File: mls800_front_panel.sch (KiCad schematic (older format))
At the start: 21 parts, among them SW10 SW_TACT_LED, SW11 SW_TACT_LED, SW2 SW_TACT_LED, SW3 SW_TACT_LED, SW4 SW_TACT_LED, SW5 SW_TACT_LED, SW6 SW_TACT_LED, SW7 SW_TACT_LED, SW8 SW_TACT_LED, SW9 SW_TACT_LED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

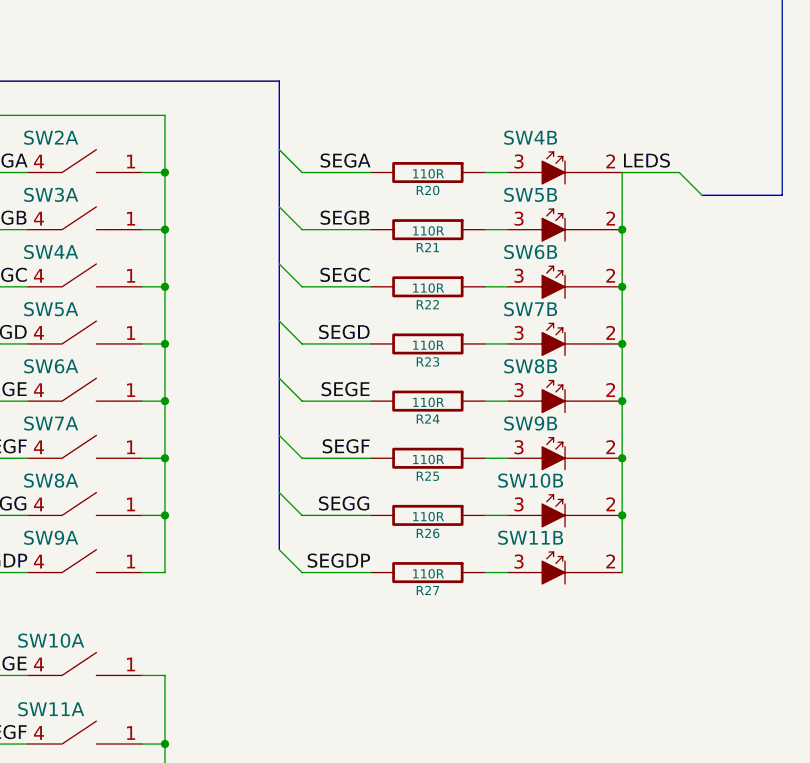
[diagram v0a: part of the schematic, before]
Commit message: MLS800
* removed front panel leds resistances
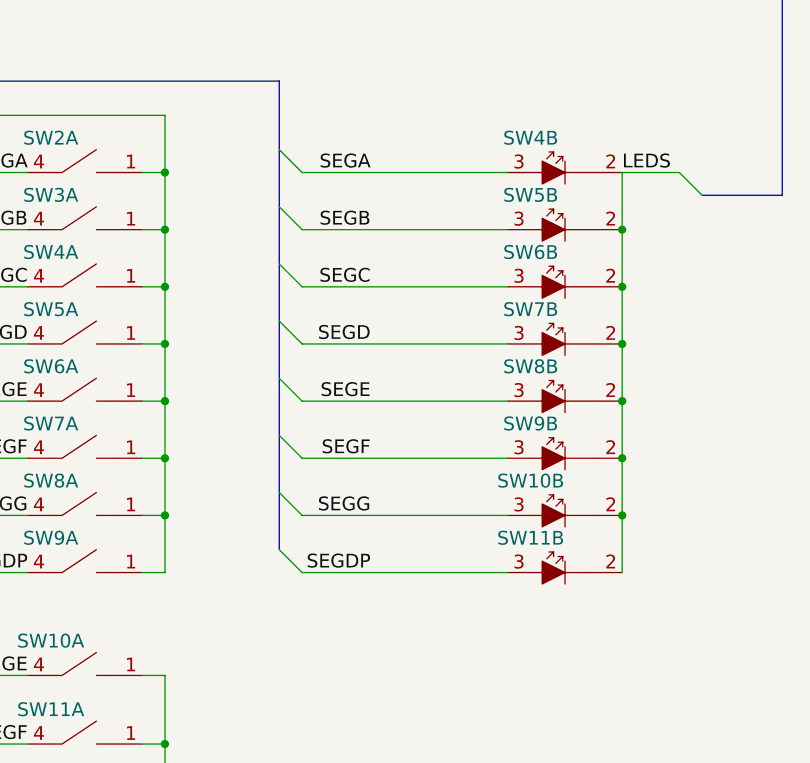
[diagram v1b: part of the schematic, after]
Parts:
- removed R20, R21, R22, R23, R24, R25, R26, R27: 110R, symbol R
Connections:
- net SEGA: now also SW4.3
- net SEGB: now also SW5.3
- net SEGC: now also SW6.3
- net SEGD: now also SW7.3
- net SEGDP: now also SW11.3
- net SEGE: now also SW8.3
- net SEGF: now also SW9.3
- net SEGG: now also SW10.3
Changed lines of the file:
@@
 Text Label 5950 5300 2    60   ~ 0
 SEGDP
-$Comp
-L R R20
-U 1 1 54406B24
-P 6200 3550
-F 0 "R20" V 6280 3550 40  0000 C CNN
-F 1 "110R" V 6207 3551 40  0000 C CNN
-F 2 "" V 6130 3550 30  0000 C CNN
-F 3 "" H 6200 3550 30  0000 C CNN
-	1    6200 3550
-	0    1    1    0
-$EndComp
-$Comp
-L R R21
-U 1 1 54408199
-P 6200 3800
-F 0 "R21" V 6280 3800 40  0000 C CNN
-F 1 "110R" V 6207 3801 40  0000 C CNN
-F 2 "" V 6130 3800 30  0000 C CNN
-F 3 "" H 6200 3800 30  0000 C CNN
-	1    6200 3800
-	0    1    1    0
-$EndComp
-$Comp
-L R R22
-U 1 1 544081CA
-P 6200 4050
-F 0 "R22" V 6280 4050 40  0000 C CNN
-F 1 "110R" V 6207 4051 40  0000 C CNN
-F 2 "" V 6130 4050 30  0000 C CNN
-F 3 "" H 6200 4050 30  0000 C CNN
-	1    6200 4050
-	0    1    1    0
-$EndComp
-$Comp
-L R R23
-U 1 1 5440822C
-P 6200 4300
-F 0 "R23" V 6280 4300 40  0000 C CNN
-F 1 "110R" V 6207 4301 40  0000 C CNN
-F 2 "" V 6130 4300 30  0000 C CNN
-F 3 "" H 6200 4300 30  0000 C CNN
-	1    6200 4300
-	0    1    1    0
-$EndComp
-$Comp
-L R R24
-U 1 1 5440826B
-P 6200 4550
-F 0 "R24" V 6280 4550 40  0000 C CNN
-F 1 "110R" V 6207 4551 40  0000 C CNN
-F 2 "" V 6130 4550 30  0000 C CNN
-F 3 "" H 6200 4550 30  0000 C CNN
-	1    6200 4550
-	0    1    1    0
-$EndComp
-$Comp
-L R R25
-U 1 1 5440829F
-P 6200 4800
-F 0 "R25" V 6280 4800 40  0000 C CNN
-F 1 "110R" V 6207 4801 40  0000 C CNN
-F 2 "" V 6130 4800 30  0000 C CNN
-F 3 "" H 6200 4800 30  0000 C CNN
-	1    6200 4800
-	0    1    1    0
-$EndComp
-$Comp
-L R R26
-U 1 1 544082E4
-P 6200 5050
-F 0 "R26" V 6280 5050 40  0000 C CNN
-F 1 "110R" V 6207 5051 40  0000 C CNN
-F 2 "" V 6130 5050 30  0000 C CNN
-F 3 "" H 6200 5050 30  0000 C CNN
-	1    6200 5050
-	0    1    1    0
-$EndComp
-$Comp
-L R R27
-U 1 1 5440831E
-P 6200 5300
-F 0 "R27" V 6280 5300 40  0000 C CNN
-F 1 "110R" V 6207 5301 40  0000 C CNN
-F 2 "" V 6130 5300 30  0000 C CNN
-F 3 "" H 6200 5300 30  0000 C CNN
-	1    6200 5300
-	0    1    1    0
-$EndComp
 Text Label 5950 4050 2    60   ~ 0
 SEGC
 Wire Wire Line
-	6550 3550 6450 3550
+	5650 3550 6550 3550
 Wire Wire Line
-	6550 3800 6450 3800
+	5650 3800 6550 3800
 Wire Wire Line
-	6550 4050 6450 4050
+	5650 4050 6550 4050
 Wire Wire Line
-	6550 4300 6450 4300
+	5650 4300 6550 4300
 Wire Wire Line
-	6550 4550 6450 4550
+	5650 4550 6550 4550
 Wire Wire Line
-	6550 4800 6450 4800
+	5650 4800 6550 4800
 Wire Wire Line
-	6550 5050 6450 5050
+	5650 5050 6550 5050
 Wire Wire Line
-	6550 5300 6450 5300
-Wire Wire Line
-	5950 3550 5650 3550
-Wire Wire Line
-	5950 3800 5650 3800
-Wire Wire Line
-	5950 4050 5650 4050
-Wire Wire Line
-	5950 4300 5650 4300
-Wire Wire Line
-	5950 4550 5650 4550
-Wire Wire Line
-	5950 4800 5650 4800
-Wire Wire Line
-	5950 5050 5650 5050
-Wire Wire Line
-	5950 5300 5650 5300
+	5650 5300 6550 5300
 Entry Wire Line
 	5550 3450 5650 3550

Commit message: MLS800
* footprint associations
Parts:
- R19: footprint (none) -> Resistors_SMD:R_0805_HandSoldering
- U5: footprint MODULE -> Housings_SSOP:SSOP-24_3.9x8.7mm_Pitch0.635mm
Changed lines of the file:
@@
 F 0 "U5" H 1950 3000 50  0000 C CNN
 F 1 "AS1115" H 2950 800 50  0000 C CNN
-F 2 "MODULE" H 2000 800 50  0001 C CNN
-F 3 "DOCUMENTATION" H 2500 1850 50  0001 C CNN
+F 2 "Housings_SSOP:SSOP-24_3.9x8.7mm_Pitch0.635mm" H 2000 800 50  0001 C CNN
+F 3 "" H 2500 1850 50  0001 C CNN
 	1    2500 1900
 	1    0    0    -1
@@
 F 0 "R19" V 1380 1050 40  0000 C CNN
 F 1 "R" V 1307 1051 40  0000 C CNN
-F 2 "" V 1230 1050 30  0000 C CNN
+F 2 "Resistors_SMD:R_0805_HandSoldering" V 1230 1050 30  0001 C CNN
 F 3 "" H 1300 1050 30  0000 C CNN
 	1    1300 1050

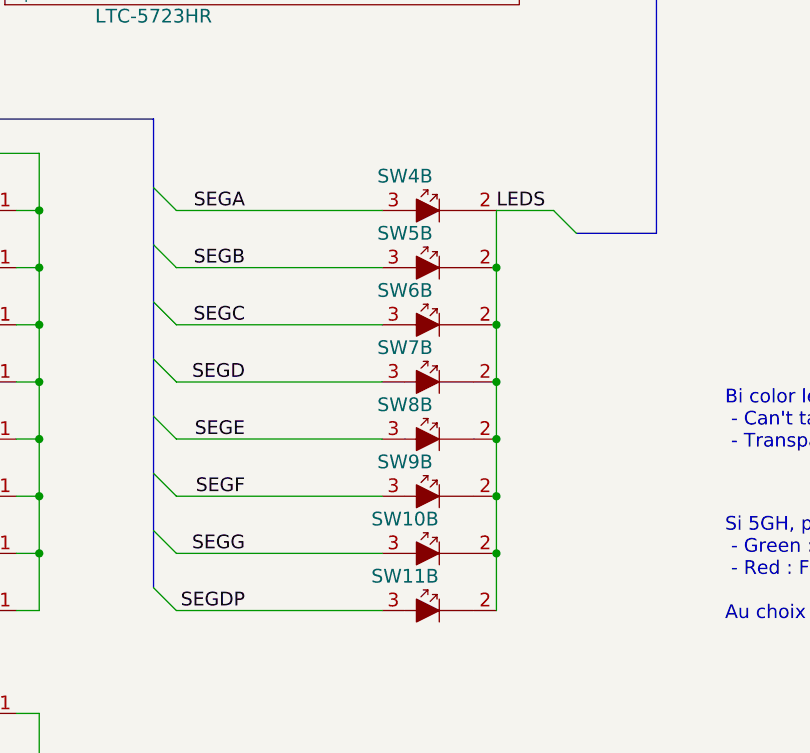
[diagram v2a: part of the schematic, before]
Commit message: MLS800
* added two news footprints
* footprint associations
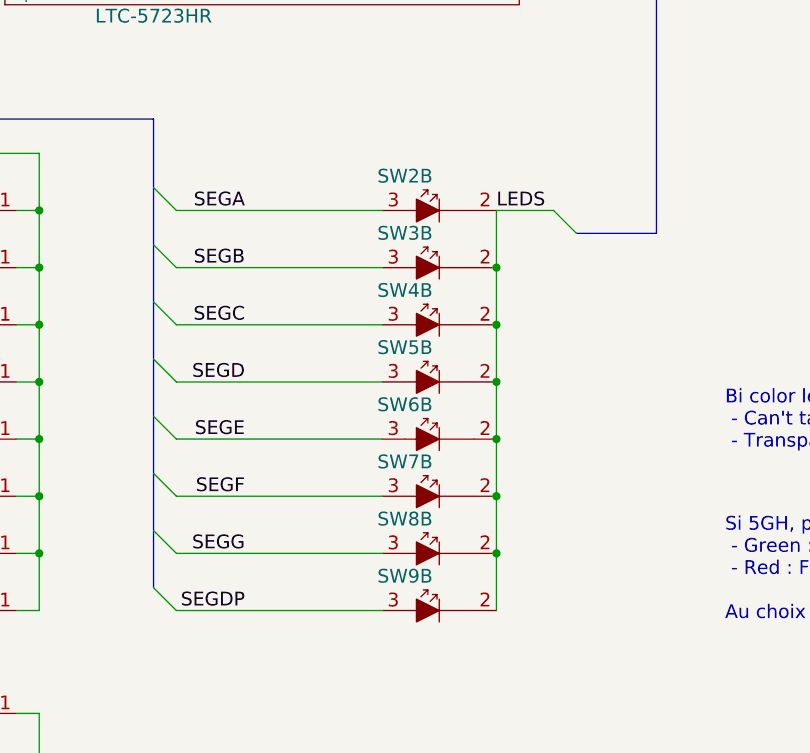
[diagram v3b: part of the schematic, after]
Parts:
- SW10, SW11, SW2, SW3, SW4, SW5, SW6, SW7, SW8, SW9: footprint (none) -> Custom-device:MEC-5G
- SW2: renamed from SW4; footprint (none) -> Custom-device:MEC-5G
- SW3: renamed from SW5; footprint (none) -> Custom-device:MEC-5G
- SW4: renamed from SW6; footprint (none) -> Custom-device:MEC-5G
- SW5: renamed from SW7; footprint (none) -> Custom-device:MEC-5G
- SW6: renamed from SW8; footprint (none) -> Custom-device:MEC-5G
- SW7: renamed from SW9; footprint (none) -> Custom-device:MEC-5G
- SW8: renamed from SW10; footprint (none) -> Custom-device:MEC-5G
- SW9: renamed from SW11; footprint (none) -> Custom-device:MEC-5G
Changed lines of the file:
@@
 LIBS:custom-micro
 LIBS:mls800-cache
-EELAYER 24 0
+EELAYER 25 0
 EELAYER END
 $Descr A4 11693 8268
@@
 F 0 "SW2" H 4550 3700 60  0000 C CNN
 F 1 "SW_TACT_LED" H 4720 3450 60  0001 C CNN
-F 2 "" H 4750 3550 60  0000 C CNN
+F 2 "Custom-device:MEC-5G" H 4750 3550 60  0001 C CNN
 F 3 "" H 4750 3550 60  0000 C CNN
 	1    4750 3550
@@
 F 0 "SW3" H 4550 3950 60  0000 C CNN
 F 1 "SW_TACT_LED" H 4720 3700 60  0001 C CNN
-F 2 "" H 4750 3800 60  0000 C CNN
+F 2 "Custom-device:MEC-5G" H 4750 3800 60  0001 C CNN
 F 3 "" H 4750 3800 60  0000 C CNN
 	1    4750 3800
@@
 F 0 "SW4" H 4550 4200 60  0000 C CNN
 F 1 "SW_TACT_LED" H 4720 3950 60  0001 C CNN
-F 2 "" H 4750 4050 60  0000 C CNN
+F 2 "Custom-device:MEC-5G" H 4750 4050 60  0001 C CNN
 F 3 "" H 4750 4050 60  0000 C CNN
 	1    4750 4050
@@
 F 0 "SW5" H 4550 4450 60  0000 C CNN
 F 1 "SW_TACT_LED" H 4720 4200 60  0001 C CNN
-F 2 "" H 4750 4300 60  0000 C CNN
+F 2 "Custom-device:MEC-5G" H 4750 4300 60  0001 C CNN
 F 3 "" H 4750 4300 60  0000 C CNN
 	1    4750 4300
@@
 F 0 "SW6" H 4550 4700 60  0000 C CNN
 F 1 "SW_TACT_LED" H 4720 4450 60  0001 C CNN
-F 2 "" H 4750 4550 60  0000 C CNN
+F 2 "Custom-device:MEC-5G" H 4750 4550 60  0001 C CNN
 F 3 "" H 4750 4550 60  0000 C CNN
 	1    4750 4550
@@
 F 0 "SW7" H 4550 4950 60  0000 C CNN
 F 1 "SW_TACT_LED" H 4720 4700 60  0001 C CNN
-F 2 "" H 4750 4800 60  0000 C CNN
+F 2 "Custom-device:MEC-5G" H 4750 4800 60  0001 C CNN
 F 3 "" H 4750 4800 60  0000 C CNN
 	1    4750 4800
@@
 F 0 "SW8" H 4550 5200 60  0000 C CNN
 F 1 "SW_TACT_LED" H 4720 4950 60  0001 C CNN
-F 2 "" H 4750 5050 60  0000 C CNN
+F 2 "Custom-device:MEC-5G" H 4750 5050 60  0001 C CNN
 F 3 "" H 4750 5050 60  0000 C CNN
 	1    4750 5050
@@
 F 0 "SW9" H 4550 5450 60  0000 C CNN
 F 1 "SW_TACT_LED" H 4720 5200 60  0001 C CNN
-F 2 "" H 4750 5300 60  0000 C CNN
+F 2 "Custom-device:MEC-5G" H 4750 5300 60  0001 C CNN
 F 3 "" H 4750 5300 60  0000 C CNN
 	1    4750 5300
@@
 	4050 2750 4050 5950
 $Comp
-L SW_TACT_LED SW4
+L SW_TACT_LED SW2
 U 2 1 54405D5F
 P 6850 3550
-F 0 "SW4" H 6650 3700 60  0000 C CNN
+F 0 "SW2" H 6650 3700 60  0000 C CNN
 F 1 "SW_TACT_LED" H 6820 3450 60  0001 C CNN
-F 2 "" H 6850 3550 60  0000 C CNN
+F 2 "Custom-device:MEC-5G" H 6850 3550 60  0001 C CNN
 F 3 "" H 6850 3550 60  0000 C CNN
 	2    6850 3550
@@
 $EndComp
 $Comp
-L SW_TACT_LED SW5
+L SW_TACT_LED SW3
 U 2 1 54405E2B
 P 6850 3800
-F 0 "SW5" H 6650 3950 60  0000 C CNN
+F 0 "SW3" H 6650 3950 60  0000 C CNN
 F 1 "SW_TACT_LED" H 6820 3700 60  0001 C CNN
-F 2 "" H 6850 3800 60  0000 C CNN
+F 2 "Custom-device:MEC-5G" H 6850 3800 60  0001 C CNN
 F 3 "" H 6850 3800 60  0000 C CNN
 	2    6850 3800
@@
 $EndComp
 $Comp
-L SW_TACT_LED SW6
+L SW_TACT_LED SW4
 U 2 1 54405E54
 P 6850 4050
-F 0 "SW6" H 6650 4200 60  0000 C CNN
+F 0 "SW4" H 6650 4200 60  0000 C CNN
 F 1 "SW_TACT_LED" H 6820 3950 60  0001 C CNN
-F 2 "" H 6850 4050 60  0000 C CNN
+F 2 "Custom-device:MEC-5G" H 6850 4050 60  0001 C CNN
 F 3 "" H 6850 4050 60  0000 C CNN
 	2    6850 4050
@@
 $EndComp
 $Comp
-L SW_TACT_LED SW7
+L SW_TACT_LED SW5
 U 2 1 54405E7E
 P 6850 4300
-F 0 "SW7" H 6650 4450 60  0000 C CNN
+F 0 "SW5" H 6650 4450 60  0000 C CNN
 F 1 "SW_TACT_LED" H 6820 4200 60  0001 C CNN
-F 2 "" H 6850 4300 60  0000 C CNN
+F 2 "Custom-device:MEC-5G" H 6850 4300 60  0001 C CNN
 F 3 "" H 6850 4300 60  0000 C CNN
 	2    6850 4300
@@
 $EndComp
 $Comp
-L SW_TACT_LED SW8
+L SW_TACT_LED SW6
 U 2 1 54405EA9
 P 6850 4550
-F 0 "SW8" H 6650 4700 60  0000 C CNN
+F 0 "SW6" H 6650 4700 60  0000 C CNN
 F 1 "SW_TACT_LED" H 6820 4450 60  0001 C CNN
-F 2 "" H 6850 4550 60  0000 C CNN
+F 2 "Custom-device:MEC-5G" H 6850 4550 60  0001 C CNN
 F 3 "" H 6850 4550 60  0000 C CNN
 	2    6850 4550
@@
 $EndComp
 $Comp
-L SW_TACT_LED SW9
+L SW_TACT_LED SW7
 U 2 1 54405ED5
 P 6850 4800
-F 0 "SW9" H 6650 4950 60  0000 C CNN
+F 0 "SW7" H 6650 4950 60  0000 C CNN
 F 1 "SW_TACT_LED" H 6820 4700 60  0001 C CNN
-F 2 "" H 6850 4800 60  0000 C CNN
+F 2 "Custom-device:MEC-5G" H 6850 4800 60  0001 C CNN
 F 3 "" H 6850 4800 60  0000 C CNN
 	2    6850 4800
@@
 $EndComp
 $Comp
-L SW_TACT_LED SW10
+L SW_TACT_LED SW8
 U 2 1 54405F27
 P 6850 5050
-F 0 "SW10" H 6650 5200 60  0000 C CNN
+F 0 "SW8" H 6650 5200 60  0000 C CNN
 F 1 "SW_TACT_LED" H 6820 4950 60  0001 C CNN
-F 2 "" H 6850 5050 60  0000 C CNN
+F 2 "Custom-device:MEC-5G" H 6850 5050 60  0001 C CNN
 F 3 "" H 6850 5050 60  0000 C CNN
 	2    6850 5050
@@
 $EndComp
 $Comp
-L SW_TACT_LED SW11
+L SW_TACT_LED SW9
 U 2 1 54405F59
 P 6850 5300
-F 0 "SW11" H 6650 5450 60  0000 C CNN
+F 0 "SW9" H 6650 5450 60  0000 C CNN
 F 1 "SW_TACT_LED" H 6820 5200 60  0001 C CNN
-F 2 "" H 6850 5300 60  0000 C CNN
+F 2 "Custom-device:MEC-5G" H 6850 5300 60  0001 C CNN
 F 3 "" H 6850 5300 60  0000 C CNN
 	2    6850 5300
@@
 F 0 "SW10" H 4550 5900 60  0000 C CNN
 F 1 "SW_TACT_LED" H 4720 5650 60  0001 C CNN
-F 2 "" H 4750 5750 60  0000 C CNN
+F 2 "Custom-device:MEC-5G" H 4750 5750 60  0001 C CNN
 F 3 "" H 4750 5750 60  0000 C CNN
 	1    4750 5750
@@
 F 0 "SW11" H 4550 6200 60  0000 C CNN
 F 1 "SW_TACT_LED" H 4720 5950 60  0001 C CNN
-F 2 "" H 4750 6050 60  0000 C CNN
+F 2 "Custom-device:MEC-5G" H 4750 6050 60  0001 C CNN
 F 3 "" H 4750 6050 60  0000 C CNN
 	1    4750 6050

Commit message: MLS800
* added two news footprints (bistable relay & simple neutrik jack)
* footprint associations
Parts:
- AFF1: footprint (none) -> Custom-display:LTC-5723
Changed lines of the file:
@@
 F 0 "AFF1" H 5450 2700 60  0000 C CNN
 F 1 "LTC-5723HR" H 5550 1800 60  0000 C CNN
-F 2 "" H 5550 2250 60  0000 C CNN
+F 2 "Custom-display:LTC-5723" H 5550 2250 60  0001 C CNN
 F 3 "" H 5550 2250 60  0000 C CNN
 	1    6050 2250

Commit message: MLS800
* started some real pcb
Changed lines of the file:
@@
 	1    0    0    -1
 $EndComp
-Entry Bus Bus
-	3950 2650 4050 2750
 Text Label 4450 3550 2    60   ~ 0
 SEGA
@@
 Connection ~ 5050 4800
 Connection ~ 5050 5050
-Wire Bus Line
-	4050 2750 4050 5950
 $Comp
 L SW_TACT_LED SW2
@@
 Wire Bus Line
 	7750 1700 7750 3650
-Entry Bus Bus
-	4050 3050 4150 3150
 Wire Bus Line
 	4150 3150 5550 3150
@@
 Wire Bus Line
 	5550 3150 5550 5200
+Wire Bus Line
+	4150 2650 4150 3150
+Wire Bus Line
+	4050 2650 4050 5950
 $EndSCHEMATC

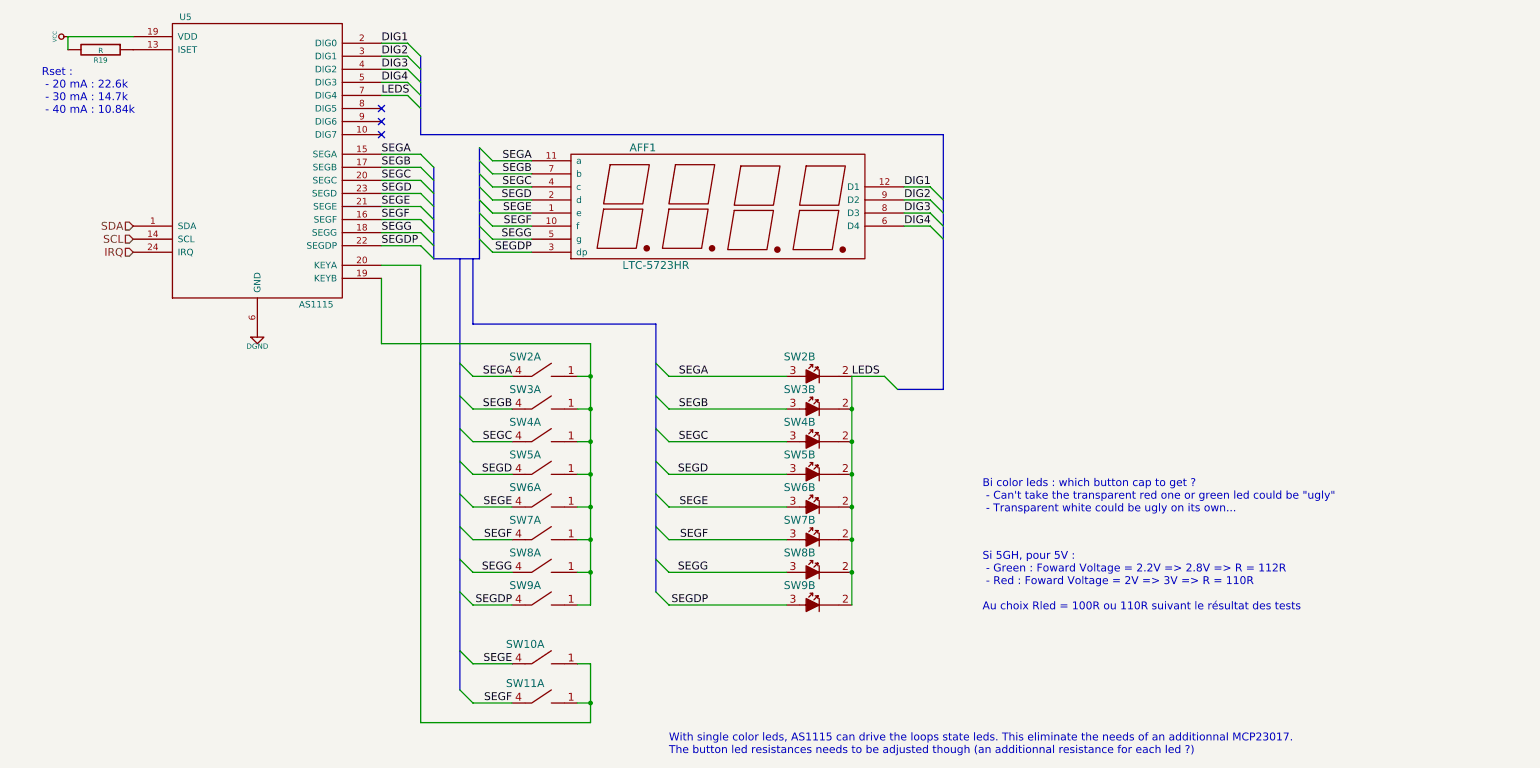
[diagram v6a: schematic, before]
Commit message: MLS800
* routing : core pcb & components
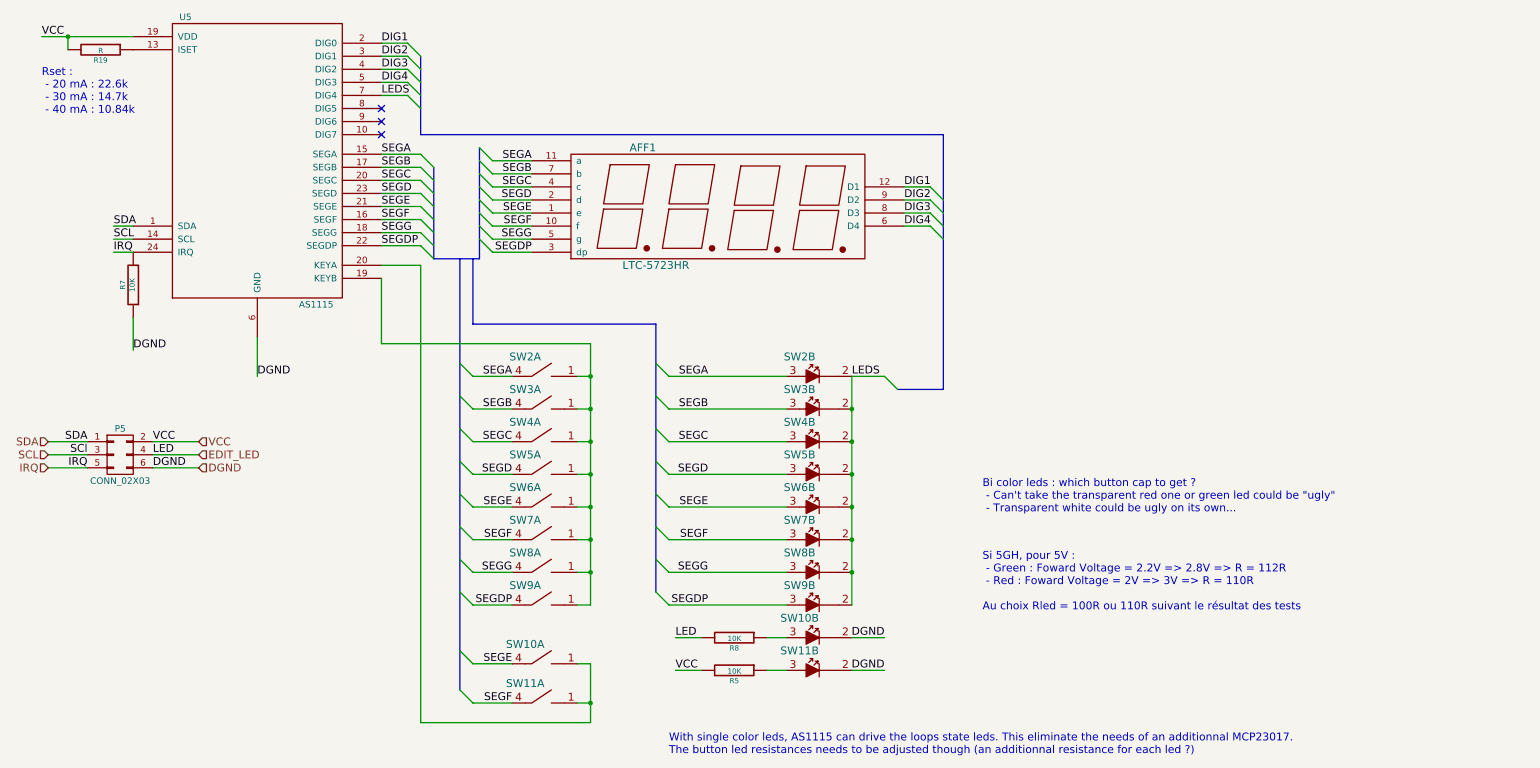
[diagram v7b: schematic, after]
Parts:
- added P5: CONN_02X03, symbol CONN_02X03
- added R5, R7, R8: 10K, symbol R
- added unit 2 of SW10
- added unit 2 of SW11
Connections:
- net DGND: now also P5.6 (P6), R7.1, SW10.2, SW11.2
- net IRQ: now also P5.5 (P5), R7.2
- net SCL: now also P5.3 (P3)
- net SDA: now also P5.1 (P1)
- net VCC: now also P5.2 (P2), R5.2
- new net: R8.1, SW10.3
- new net: R5.1, SW11.3
- new net EDIT_LED: P5.4 (P4), R8.2

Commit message: MLS800
* schematic : added pin header for board connectivity & moved some parts to the front panel layout
* routing : core pcb & components
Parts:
- P5: footprint (none) -> Pin_Headers:Pin_Header_Straight_2x03
- R5, R7, R8: footprint (none) -> Resistors_SMD:R_0805_HandSoldering
- SW10, SW11: footprint (none) -> Custom-device:MEC-5G
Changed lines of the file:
@@
 F 0 "R8" V 6230 5550 40  0000 C CNN
 F 1 "10K" V 6157 5551 40  0000 C CNN
-F 2 "" V 6080 5550 30  0000 C CNN
+F 2 "Resistors_SMD:R_0805_HandSoldering" H 6080 5550 30  0001 C CNN
 F 3 "" H 6150 5550 30  0000 C CNN
 	1    6150 5550
@@
 F 0 "SW10" H 6650 5700 60  0000 C CNN
 F 1 "SW_TACT_LED" H 6820 5450 60  0001 C CNN
-F 2 "" H 6850 5550 60  0000 C CNN
+F 2 "Custom-device:MEC-5G" H 6850 5550 60  0001 C CNN
 F 3 "" H 6850 5550 60  0000 C CNN
 	2    6850 5550
@@
 F 0 "R5" V 6230 5800 40  0000 C CNN
 F 1 "10K" V 6157 5801 40  0000 C CNN
-F 2 "" V 6080 5800 30  0000 C CNN
+F 2 "Resistors_SMD:R_0805_HandSoldering" H 6080 5800 30  0001 C CNN
 F 3 "" H 6150 5800 30  0000 C CNN
 	1    6150 5800
@@
 F 0 "SW11" H 6650 5950 60  0000 C CNN
 F 1 "SW_TACT_LED" H 6820 5700 60  0001 C CNN
-F 2 "" H 6850 5800 60  0000 C CNN
+F 2 "Custom-device:MEC-5G" H 6850 5800 60  0001 C CNN
 F 3 "" H 6850 5800 60  0000 C CNN
 	2    6850 5800
@@
 F 0 "R7" V 1630 2850 40  0000 C CNN
 F 1 "10K" V 1557 2851 40  0000 C CNN
-F 2 "" V 1480 2850 30  0000 C CNN
+F 2 "Resistors_SMD:R_0805_HandSoldering" V 1480 2850 30  0001 C CNN
 F 3 "" H 1550 2850 30  0000 C CNN
 	1    1550 2850
@@
 F 0 "P5" H 1450 4350 50  0000 C CNN
 F 1 "CONN_02X03" H 1450 3950 50  0000 C CNN
-F 2 "" H 1450 2950 60  0000 C CNN
+F 2 "Pin_Headers:Pin_Header_Straight_2x03" H 1450 2950 60  0001 C CNN
 F 3 "" H 1450 2950 60  0000 C CNN
 	1    1450 4150
